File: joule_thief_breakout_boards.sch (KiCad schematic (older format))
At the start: 37 parts, among them J1 Conn_01x02, J10 Conn_01x02, J11 Voltage, J12 Current, J13 Light, J2 Conn_01x02, J3 Conn_01x02, J4 Conn_01x02, J5 Conn_01x02, J6 Conn_01x03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

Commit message: add schematic notes for sensors
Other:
- note added: "5V 100mA max from DI-1110 datalogger\n Voltage is unregulated from USB\n INA180 draws worst case 300uA\n TEMT600 draws worst case 330uA\n NCP1117 drop out is 0.8V at low current"
- note added: "TEMT600 Light Sensor Breakout from Sparkfun or similar.\nSensor is placed above a single LED with cover to prevent ambient light readings"
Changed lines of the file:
@@
 Wire Notes Line
 	2500 2300 8300 2300
+Text Notes 4050 3050 0    60   ~ 0
+5V 100mA max from DI-1110 datalogger\n    Voltage is unregulated from USB\n    INA180 draws worst case 300uA\n    TEMT600 draws worst case 330uA\n    NCP1117 drop out is 0.8V at low current
+Text Notes 6600 5650 0    60   ~ 0
+TEMT600 Light Sensor Breakout from Sparkfun or similar.\nSensor is placed above a single LED with cover to prevent ambient light readings
 $EndSCHEMATC

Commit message: Specify gain of INA180 as A4 (200) for joule thief with sensors
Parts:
- U3: value INA180 -> INA180A4; Description (none) -> NONE; Manufacture (none) -> NONE; Mfg Part Number (none) -> NONE; Package (none) -> NONE
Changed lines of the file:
@@
 P 4550 4500
 F 0 "U3" H 4850 4100 60  0000 C CNN
-F 1 "INA180" H 4250 4900 60  0000 C CNN
+F 1 "INA180A4" H 4250 4900 60  0000 C CNN
 F 2 "TO_SOT_Packages_SMD:TSOT-23-5_HandSoldering" H 4550 4500 60  0001 C CNN
 F 3 "" H 4550 4500 60  0001 C CNN
+F 4 "NONE" H 4550 4500 60  0001 C CNN "Manufacture"
+F 5 "NONE" H 4550 4500 60  0001 C CNN "Mfg Part Number"
+F 6 "NONE" H 4550 4500 60  0001 C CNN "Package"
+F 7 "NONE" H 4550 4500 60  0001 C CNN "Description"
 	1    4550 4500
 	1    0    0    -1

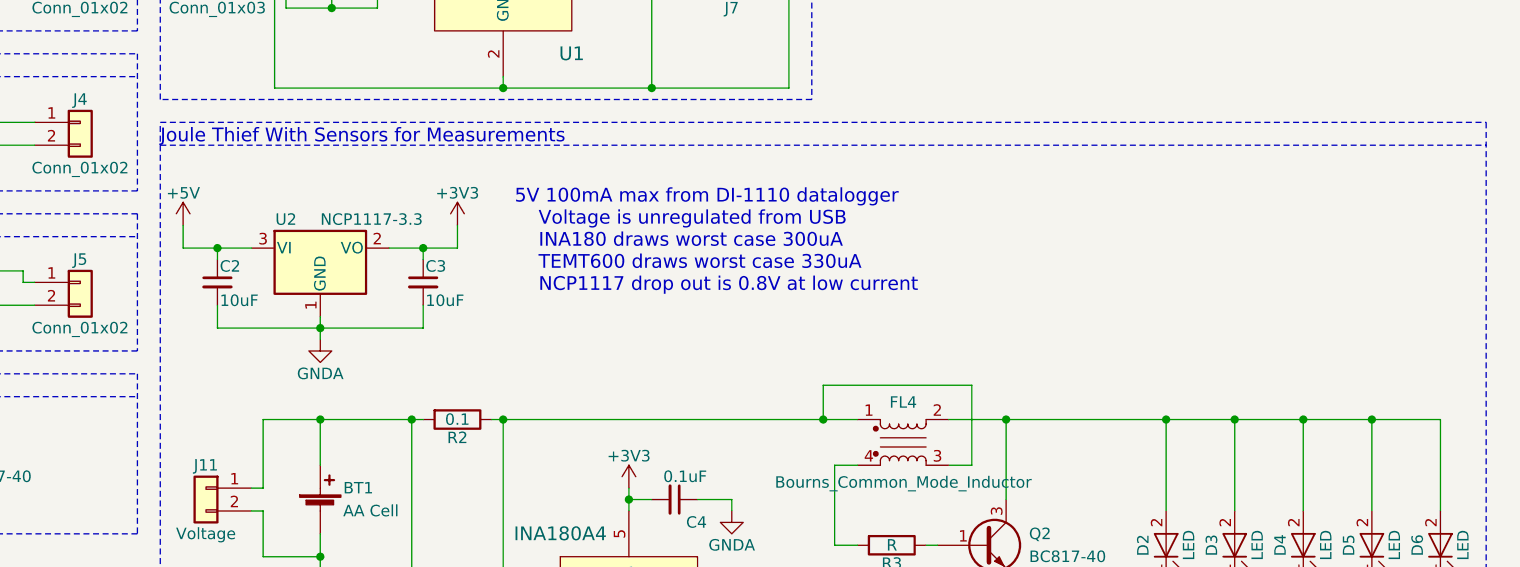
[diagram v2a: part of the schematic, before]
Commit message: add header for sensor 5V power
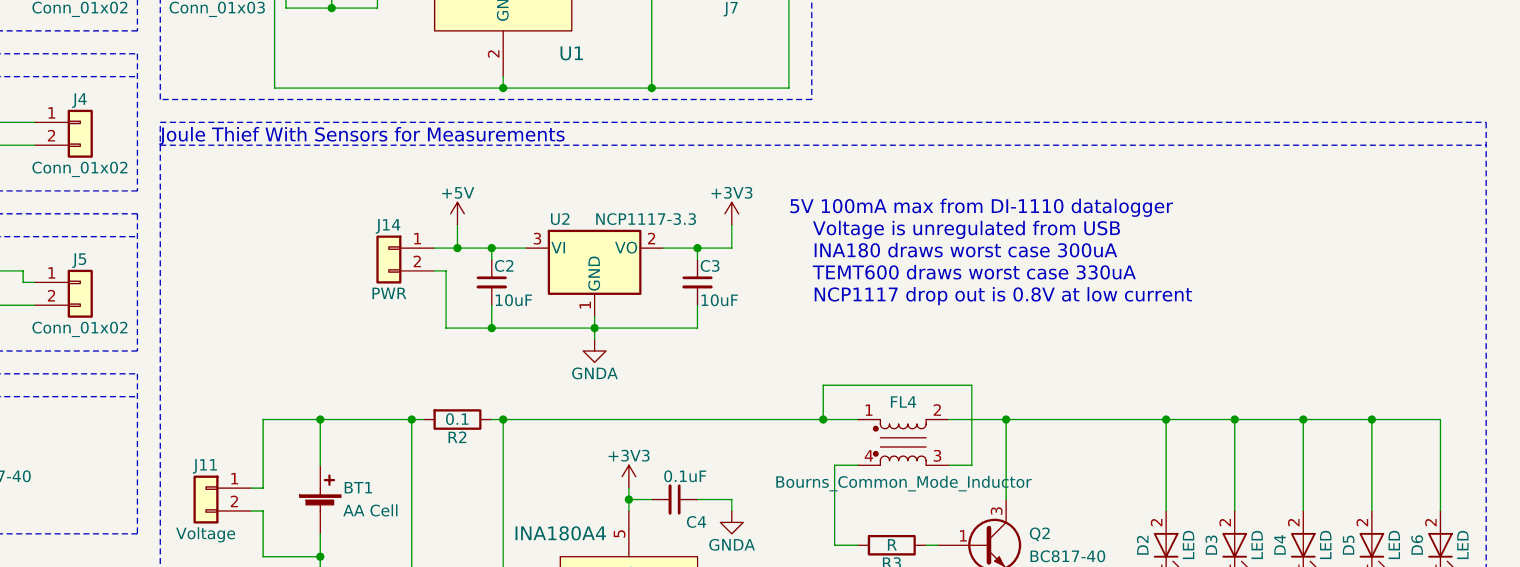
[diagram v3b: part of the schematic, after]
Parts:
- added J14: PWR, Pin_Headers:Pin_Header_Straight_2x01_Pitch2.54mm, symbol Conn_01x02
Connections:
- net +5V: now also J14.1 (Pin_1)
- net GNDA: now also J14.2 (Pin_2)
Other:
- moved on the sheet: C2, C3, U2
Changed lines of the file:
@@
 L NCP1117-3.3_TO252 U2
 U 1 1 59E2F8B1
-P 3200 2850
-F 0 "U2" H 3050 2975 50  0000 C CNN
-F 1 "NCP1117-3.3" H 3200 2975 50  0000 L CNN
-F 2 "TO_SOT_Packages_SMD:TO-252-2" H 3200 3075 50  0001 C CNN
-F 3 "" H 3200 2850 50  0001 C CNN
-	1    3200 2850
+P 4400 2850
+F 0 "U2" H 4250 2975 50  0000 C CNN
+F 1 "NCP1117-3.3" H 4400 2975 50  0000 L CNN
+F 2 "TO_SOT_Packages_SMD:TO-252-2" H 4400 3075 50  0001 C CNN
+F 3 "" H 4400 2850 50  0001 C CNN
+	1    4400 2850
 	1    0    0    -1
 $EndComp
@@
 L +5V #PWR03
 U 1 1 59E34F97
-P 2600 2750
-F 0 "#PWR03" H 2600 2600 50  0001 C CNN
-F 1 "+5V" H 2600 2890 50  0000 C CNN
-F 2 "" H 2600 2750 50  0001 C CNN
-F 3 "" H 2600 2750 50  0001 C CNN
-	1    2600 2750
-	1    0    0    -1
-$EndComp
-$Comp
-L C_Small C2
-U 1 1 59E351B3
-P 2750 3000
-F 0 "C2" H 2760 3070 50  0000 L CNN
-F 1 "10uF" H 2760 2920 50  0000 L CNN
-F 2 "Capacitors_SMD:C_0805_HandSoldering" H 2750 3000 50  0001 C CNN
-F 3 "" H 2750 3000 50  0001 C CNN
-F 4 "NONE" H 2750 3000 60  0001 C CNN "Manufacture"
-F 5 "NONE" H 2750 3000 60  0001 C CNN "Mfg Part Number"
-F 6 "NONE" H 2750 3000 60  0001 C CNN "Package"
-F 7 "NONE" H 2750 3000 60  0001 C CNN "Description"
-	1    2750 3000
-	1    0    0    -1
-$EndComp
-$Comp
-L C_Small C3
-U 1 1 59E35220
-P 3650 3000
-F 0 "C3" H 3660 3070 50  0000 L CNN
-F 1 "10uF" H 3660 2920 50  0000 L CNN
-F 2 "Capacitors_SMD:C_0805_HandSoldering" H 3650 3000 50  0001 C CNN
-F 3 "" H 3650 3000 50  0001 C CNN
-F 4 "NONE" H 3650 3000 60  0001 C CNN "Manufacture"
-F 5 "NONE" H 3650 3000 60  0001 C CNN "Mfg Part Number"
-F 6 "NONE" H 3650 3000 60  0001 C CNN "Package"
-F 7 "NONE" H 3650 3000 60  0001 C CNN "Description"
-	1    3650 3000
-	1    0    0    -1
-$EndComp
-$Comp
-L GNDA #PWR04
-U 1 1 59E35B65
-P 3200 3250
-F 0 "#PWR04" H 3200 3000 50  0001 C CNN
-F 1 "GNDA" H 3200 3100 50  0000 C CNN
-F 2 "" H 3200 3250 50  0001 C CNN
-F 3 "" H 3200 3250 50  0001 C CNN
-	1    3200 3250
-	1    0    0    -1
-$EndComp
-$Comp
-L +3V3 #PWR05
-U 1 1 59E368E8
 P 3800 2750
-F 0 "#PWR05" H 3800 2600 50  0001 C CNN
-F 1 "+3V3" H 3800 2890 50  0000 C CNN
+F 0 "#PWR03" H 3800 2600 50  0001 C CNN
+F 1 "+5V" H 3800 2890 50  0000 C CNN
 F 2 "" H 3800 2750 50  0001 C CNN
 F 3 "" H 3800 2750 50  0001 C CNN
 	1    3800 2750
+	1    0    0    -1
+$EndComp
+$Comp
+L C_Small C2
+U 1 1 59E351B3
+P 3950 3000
+F 0 "C2" H 3960 3070 50  0000 L CNN
+F 1 "10uF" H 3960 2920 50  0000 L CNN
+F 2 "Capacitors_SMD:C_0805_HandSoldering" H 3950 3000 50  0001 C CNN
+F 3 "" H 3950 3000 50  0001 C CNN
+F 4 "NONE" H 3950 3000 60  0001 C CNN "Manufacture"
+F 5 "NONE" H 3950 3000 60  0001 C CNN "Mfg Part Number"
+F 6 "NONE" H 3950 3000 60  0001 C CNN "Package"
+F 7 "NONE" H 3950 3000 60  0001 C CNN "Description"
+	1    3950 3000
+	1    0    0    -1
+$EndComp
+$Comp
+L C_Small C3
+U 1 1 59E35220
+P 4850 3000
+F 0 "C3" H 4860 3070 50  0000 L CNN
+F 1 "10uF" H 4860 2920 50  0000 L CNN
+F 2 "Capacitors_SMD:C_0805_HandSoldering" H 4850 3000 50  0001 C CNN
+F 3 "" H 4850 3000 50  0001 C CNN
+F 4 "NONE" H 4850 3000 60  0001 C CNN "Manufacture"
+F 5 "NONE" H 4850 3000 60  0001 C CNN "Mfg Part Number"
+F 6 "NONE" H 4850 3000 60  0001 C CNN "Package"
+F 7 "NONE" H 4850 3000 60  0001 C CNN "Description"
+	1    4850 3000
+	1    0    0    -1
+$EndComp
+$Comp
+L GNDA #PWR04
+U 1 1 59E35B65
+P 4400 3250
+F 0 "#PWR04" H 4400 3000 50  0001 C CNN
+F 1 "GNDA" H 4400 3100 50  0000 C CNN
+F 2 "" H 4400 3250 50  0001 C CNN
+F 3 "" H 4400 3250 50  0001 C CNN
+	1    4400 3250
+	1    0    0    -1
+$EndComp
+$Comp
+L +3V3 #PWR05
+U 1 1 59E368E8
+P 5000 2750
+F 0 "#PWR05" H 5000 2600 50  0001 C CNN
+F 1 "+3V3" H 5000 2890 50  0000 C CNN
+F 2 "" H 5000 2750 50  0001 C CNN
+F 3 "" H 5000 2750 50  0001 C CNN
+	1    5000 2750
 	1    0    0    -1
 $EndComp
@@
 Connection ~ 6900 4450
 Wire Wire Line
-	3200 3150 3200 3250
-Wire Wire Line
-	3500 2850 3800 2850
-Wire Wire Line
-	3650 2850 3650 2900
-Wire Wire Line
-	3650 3200 3650 3100
-Wire Wire Line
-	2750 3200 3650 3200
-Connection ~ 3200 3200
-Wire Wire Line
-	2750 3100 2750 3200
-Wire Wire Line
-	2600 2850 2900 2850
-Wire Wire Line
-	2600 2850 2600 2750
-Wire Wire Line
-	2750 2900 2750 2850
-Connection ~ 2750 2850
+	4400 3150 4400 3250
+Wire Wire Line
+	4700 2850 5000 2850
+Wire Wire Line
+	4850 2850 4850 2900
+Wire Wire Line
+	4850 3200 4850 3100
+Wire Wire Line
+	3750 3200 4850 3200
+Connection ~ 4400 3200
+Wire Wire Line
+	3950 3100 3950 3200
+Wire Wire Line
+	3700 2850 4100 2850
 Wire Wire Line
 	3800 2850 3800 2750
-Connection ~ 3650 2850
+Wire Wire Line
+	3950 2900 3950 2850
+Connection ~ 3950 2850
+Wire Wire Line
+	5000 2850 5000 2750
+Connection ~ 4850 2850
 Wire Wire Line
 	4550 3900 4550 4000
@@
 Wire Notes Line
 	2500 2300 8300 2300
-Text Notes 4050 3050 0    60   ~ 0
+Text Notes 5250 3100 0    60   ~ 0
 5V 100mA max from DI-1110 datalogger\n    Voltage is unregulated from USB\n    INA180 draws worst case 300uA\n    TEMT600 draws worst case 330uA\n    NCP1117 drop out is 0.8V at low current
 Text Notes 6600 5650 0    60   ~ 0
 TEMT600 Light Sensor Breakout from Sparkfun or similar.\nSensor is placed above a single LED with cover to prevent ambient light readings
+$Comp
+L Conn_01x02 J14
+U 1 1 59E367EB
+P 3500 2850
+F 0 "J14" H 3500 2950 50  0000 C CNN
+F 1 "PWR" H 3500 2650 50  0000 C CNN
+F 2 "Pin_Headers:Pin_Header_Straight_2x01_Pitch2.54mm" H 3500 2850 50  0001 C CNN
+F 3 "" H 3500 2850 50  0001 C CNN
+F 4 "NONE" H 3500 2850 60  0001 C CNN "Manufacture"
+F 5 "NONE" H 3500 2850 60  0001 C CNN "Mfg Part Number"
+F 6 "NONE" H 3500 2850 60  0001 C CNN "Package"
+F 7 "NONE" H 3500 2850 60  0001 C CNN "Description"
+	1    3500 2850
+	-1   0    0    -1
+$EndComp
+Connection ~ 3800 2850
+Wire Wire Line
+	3700 2950 3750 2950
+Wire Wire Line
+	3750 2950 3750 3200
+Connection ~ 3950 3200
 $EndSCHEMATC

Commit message: update pin header footprints for new board to use etch footprint
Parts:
- A1: footprint Pin_Headers:Pin_Header_Straight_1x03_Pitch2.54mm -> lib_fp:Etch_Pin_Header_Straight_1x03_Pitch2.54mm
- J11, J12, J13, J14: footprint Pin_Headers:Pin_Header_Straight_2x01_Pitch2.54mm -> lib_fp:Etch_Pin_Header_Straight_1x02_Pitch2.54mm
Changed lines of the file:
@@
 F 0 "J12" H 5350 4600 50  0000 C CNN
 F 1 "Current" H 5350 4300 50  0000 C CNN
-F 2 "Pin_Headers:Pin_Header_Straight_2x01_Pitch2.54mm" H 5350 4500 50  0001 C CNN
+F 2 "lib_fp:Etch_Pin_Header_Straight_1x02_Pitch2.54mm" H 5350 4500 50  0001 C CNN
 F 3 "" H 5350 4500 50  0001 C CNN
 F 4 "NONE" H 5350 4500 60  0001 C CNN "Manufacture"
@@
 F 0 "J11" H 2700 4000 50  0000 C CNN
 F 1 "Voltage" H 2700 3700 50  0000 C CNN
-F 2 "Pin_Headers:Pin_Header_Straight_2x01_Pitch2.54mm" H 2700 3900 50  0001 C CNN
+F 2 "lib_fp:Etch_Pin_Header_Straight_1x02_Pitch2.54mm" H 2700 3900 50  0001 C CNN
 F 3 "" H 2700 3900 50  0001 C CNN
 F 4 "NONE" H 2700 3900 60  0001 C CNN "Manufacture"
@@
 F 0 "A1" H 7350 4850 60  0000 C CNN
 F 1 "TEMT600" H 7350 5250 60  0000 C CNN
-F 2 "Pin_Headers:Pin_Header_Straight_1x03_Pitch2.54mm" H 7350 5050 60  0001 C CNN
+F 2 "lib_fp:Etch_Pin_Header_Straight_1x03_Pitch2.54mm" H 7350 5050 60  0001 C CNN
 F 3 "" H 7350 5050 60  0001 C CNN
 	1    7350 5050
@@
 F 0 "J13" H 8050 5150 50  0000 C CNN
 F 1 "Light" H 8050 4850 50  0000 C CNN
-F 2 "Pin_Headers:Pin_Header_Straight_2x01_Pitch2.54mm" H 8050 5050 50  0001 C CNN
+F 2 "lib_fp:Etch_Pin_Header_Straight_1x02_Pitch2.54mm" H 8050 5050 50  0001 C CNN
 F 3 "" H 8050 5050 50  0001 C CNN
 F 4 "NONE" H 8050 5050 60  0001 C CNN "Manufacture"
@@
 F 0 "J14" H 3500 2950 50  0000 C CNN
 F 1 "PWR" H 3500 2650 50  0000 C CNN
-F 2 "Pin_Headers:Pin_Header_Straight_2x01_Pitch2.54mm" H 3500 2850 50  0001 C CNN
+F 2 "lib_fp:Etch_Pin_Header_Straight_1x02_Pitch2.54mm" H 3500 2850 50  0001 C CNN
 F 3 "" H 3500 2850 50  0001 C CNN
 F 4 "NONE" H 3500 2850 60  0001 C CNN "Manufacture"

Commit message: set value of R3
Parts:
- R3: value R -> 6.8K; Description (none) -> NONE; Manufacture (none) -> NONE; Mfg Part Number (none) -> NONE; Package (none) -> NONE
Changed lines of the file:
@@
 P 5700 4150
 F 0 "R3" V 5780 4150 50  0000 C CNN
-F 1 "R" V 5700 4150 50  0000 C CNN
+F 1 "6.8K" V 5700 4150 50  0000 C CNN
 F 2 "Resistors_SMD:R_0805_HandSoldering" V 5630 4150 50  0001 C CNN
 F 3 "" H 5700 4150 50  0001 C CNN
+F 4 "NONE" H 5700 4150 60  0001 C CNN "Manufacture"
+F 5 "NONE" H 5700 4150 60  0001 C CNN "Mfg Part Number"
+F 6 "NONE" H 5700 4150 60  0001 C CNN "Package"
+F 7 "NONE" H 5700 4150 60  0001 C CNN "Description"
 	1    5700 4150
 	0    1    1    0
